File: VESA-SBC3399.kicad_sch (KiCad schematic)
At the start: 0 parts

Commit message: generate schematic
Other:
- added sheet CPU-RK3399 (CPU-RK3399.kicad_sch)
- added sheet Camera (Camera.kicad_sch)
- added sheet Ethernet PHY (PHY.kicad_sch)
- added sheet HDMI Port (HDMI.kicad_sch)
- added sheet PCIe M.2 M-Key (PCIe.kicad_sch)
- added sheet USB 2.0 Type-A0 (USBA0.kicad_sch)
- added sheet USB 2.0 Type-A1 (USBA1.kicad_sch)
- added sheet USB 3.0 Type-C0 (USBC0.kicad_sch)
- added sheet USB 3.0 Type-C1 (USBC1.kicad_sch)
- added sheet micro SD Card (microSD.kicad_sch)
- title: (none) -> VESA-SBC3399

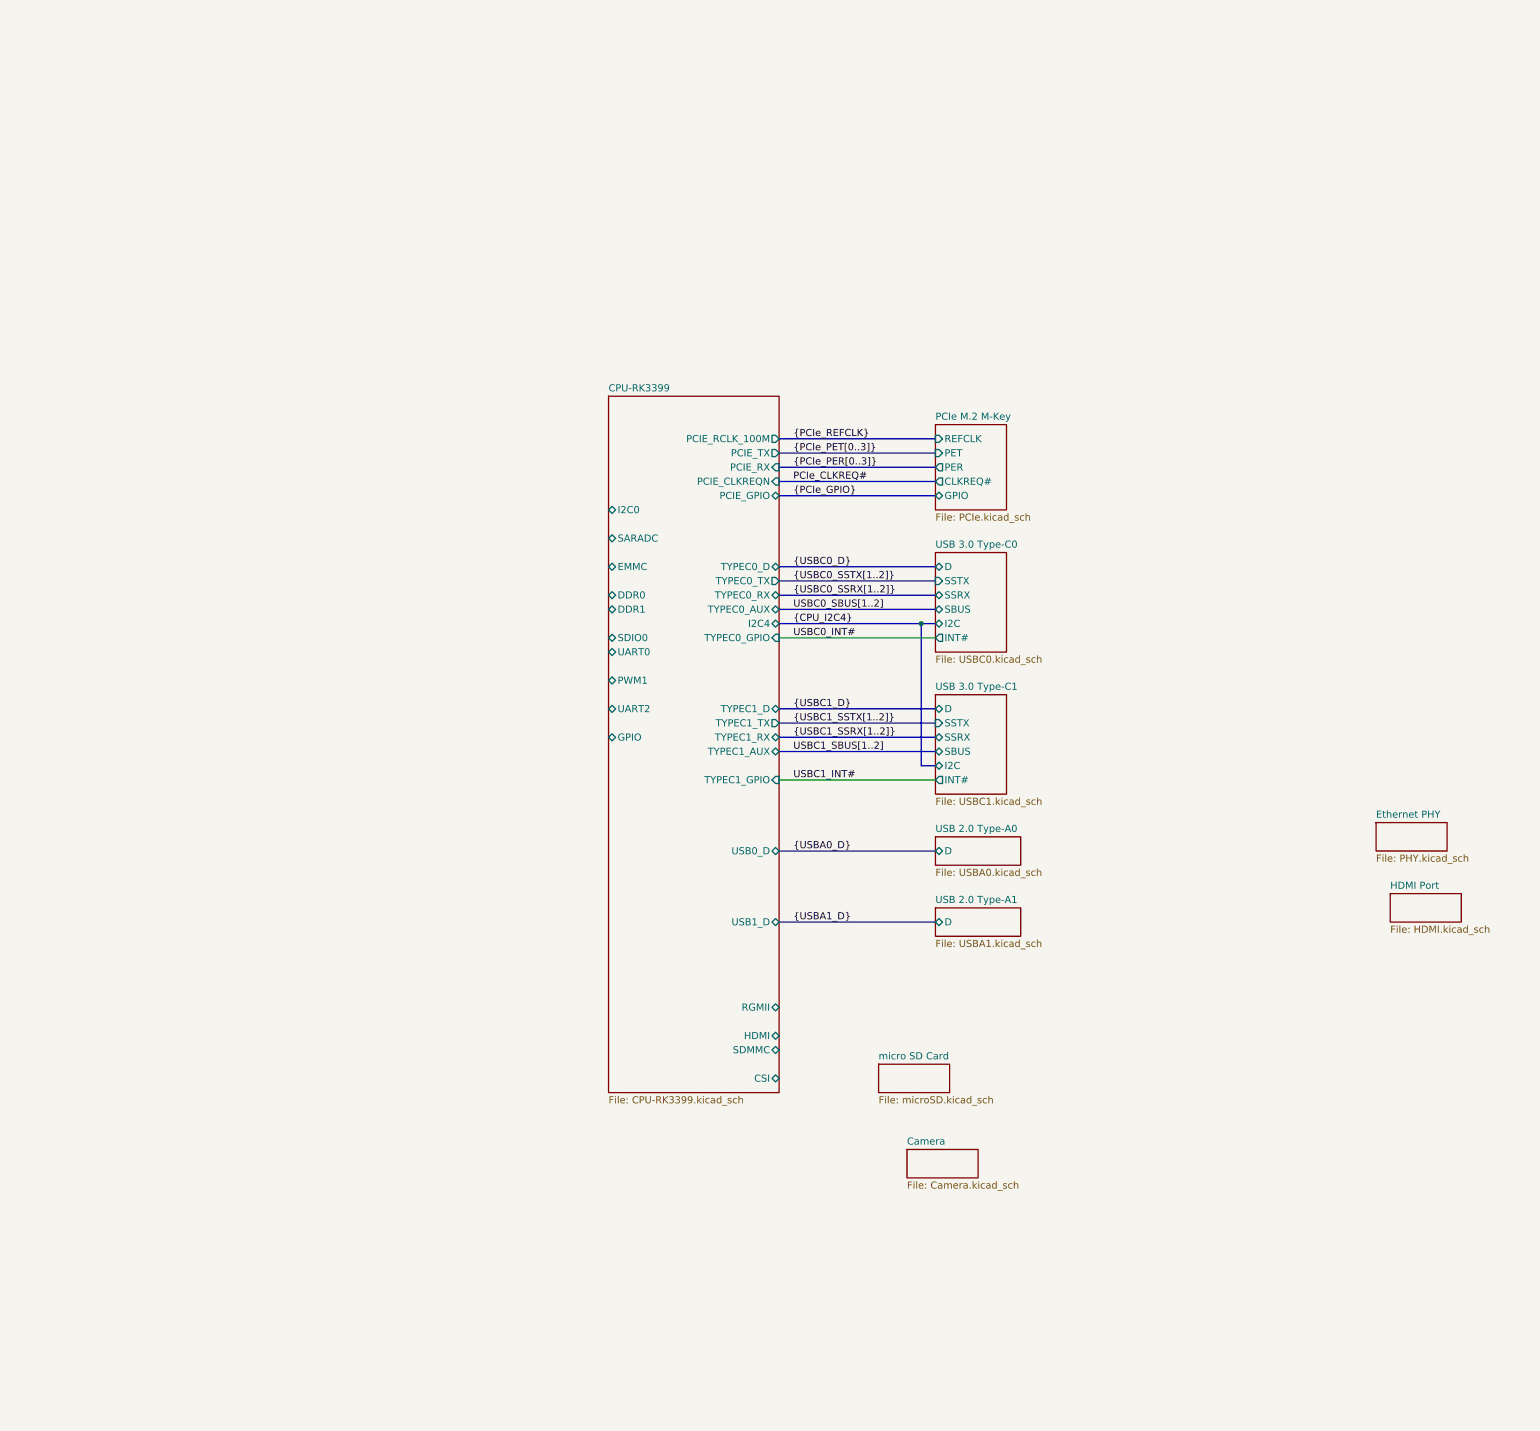
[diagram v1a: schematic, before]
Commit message: update schematic
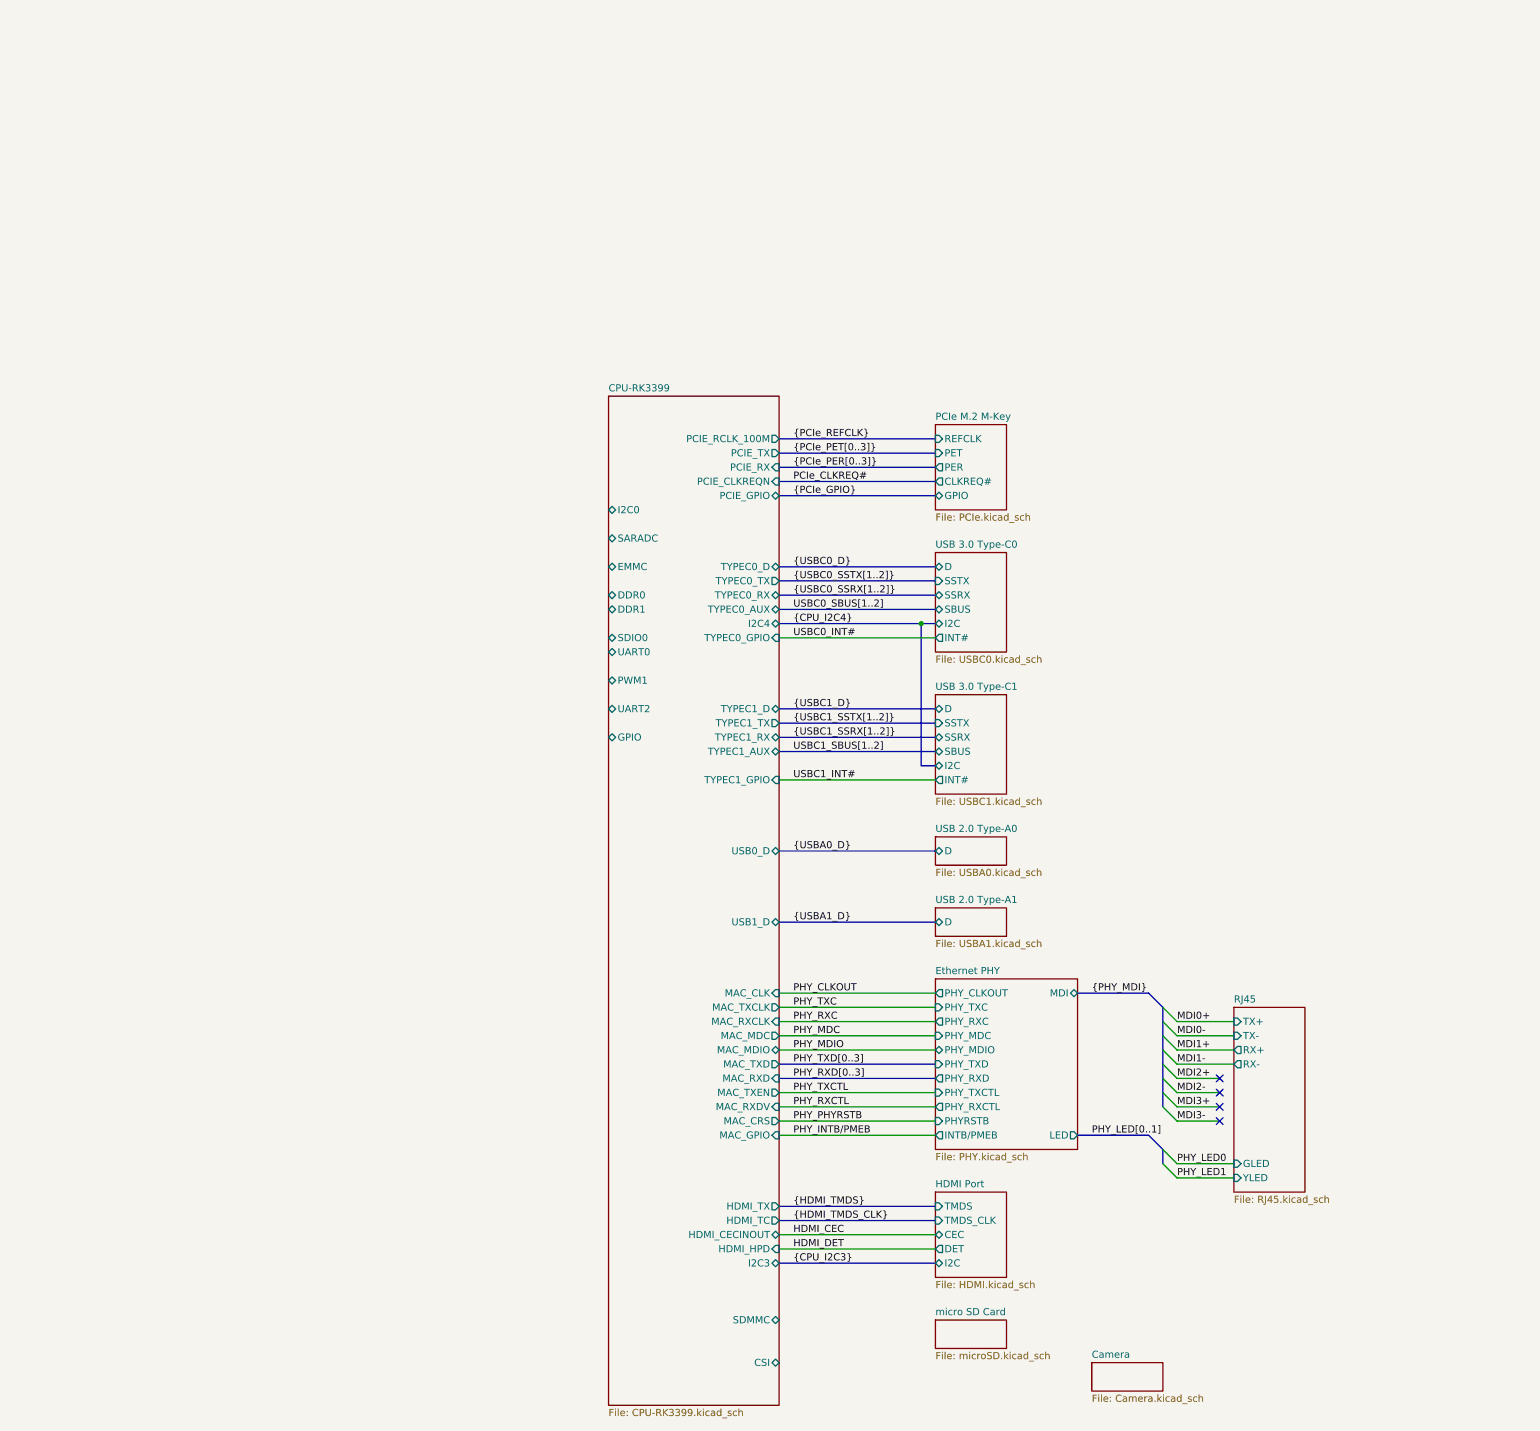
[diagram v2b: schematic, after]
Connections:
- no-connect marks 0 -> 4
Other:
- added sheet RJ45 (RJ45.kicad_sch)
- sheet CPU-RK3399 ports: added HDMI_CECINOUT, HDMI_HPD, HDMI_TC, HDMI_TX, I2C3, MAC_CLK, MAC_CRS, MAC_GPIO, MAC_MDC, MAC_MDIO, MAC_RXCLK, MAC_RXD, MAC_RXDV, MAC_TXCLK, MAC_TXD, MAC_TXEN; removed HDMI, RGMII
- sheet Ethernet PHY ports: added INTB/PMEB, LED, MDI, PHYRSTB, PHY_CLKOUT, PHY_MDC, PHY_MDIO, PHY_RXC, PHY_RXCTL, PHY_RXD, PHY_TXC, PHY_TXCTL, PHY_TXD; removed none
- sheet HDMI Port ports: added CEC, DET, I2C, TMDS, TMDS_CLK; removed none

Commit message: update root schematic
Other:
- added sheet Cooling Fan (FAN.kicad_sch)
- added sheet DDR3L RAM0 (RAM0.kicad_sch)
- added sheet DDR3L RAM1 (RAM1.kicad_sch)
- added sheet Power (Power.kicad_sch)
- added sheet WiFi_BLE (WiFi_BLE.kicad_sch)
- added sheet eMMC Flash (eMMC.kicad_sch)
- sheet CPU-RK3399 ports: added CAM_GPIO, DDR0_A, DDR0_BA, DDR0_CASN, DDR0_CKE, DDR0_CLK, DDR0_CSN, DDR0_DM, DDR0_DQ, DDR0_DQS, DDR0_ODT, DDR0_RASN, DDR0_RESETN, DDR0_WEN, DDR1_A, DDR1_BA, DDR1_CASN, DDR1_CKE, DDR1_CLK, DDR1_CSN, DDR1_DM, DDR1_DQ, DDR1_DQS, DDR1_ODT, DDR1_RASN, DDR1_RESETN, DDR1_WEN, EMMC_CLK, EMMC_CMD, EMMC_DATA, EMMC_STRB, FAN_GPIO, I2C1, MIPI_RX0_CLK, MIPI_RX0_D, SDMMC0_CLKOUT, SDMMC0_CMD, SDMMC0_D, SDMMC0_DET#, WLBT_GPIO; removed CSI, DDR0, DDR1, SDMMC
- sheet Camera ports: added CSI1_D, DSI_C, I2C, MCLK, PDN, RST; removed none
- sheet micro SD Card ports: added CD, CLX, CMD, DAT; removed none

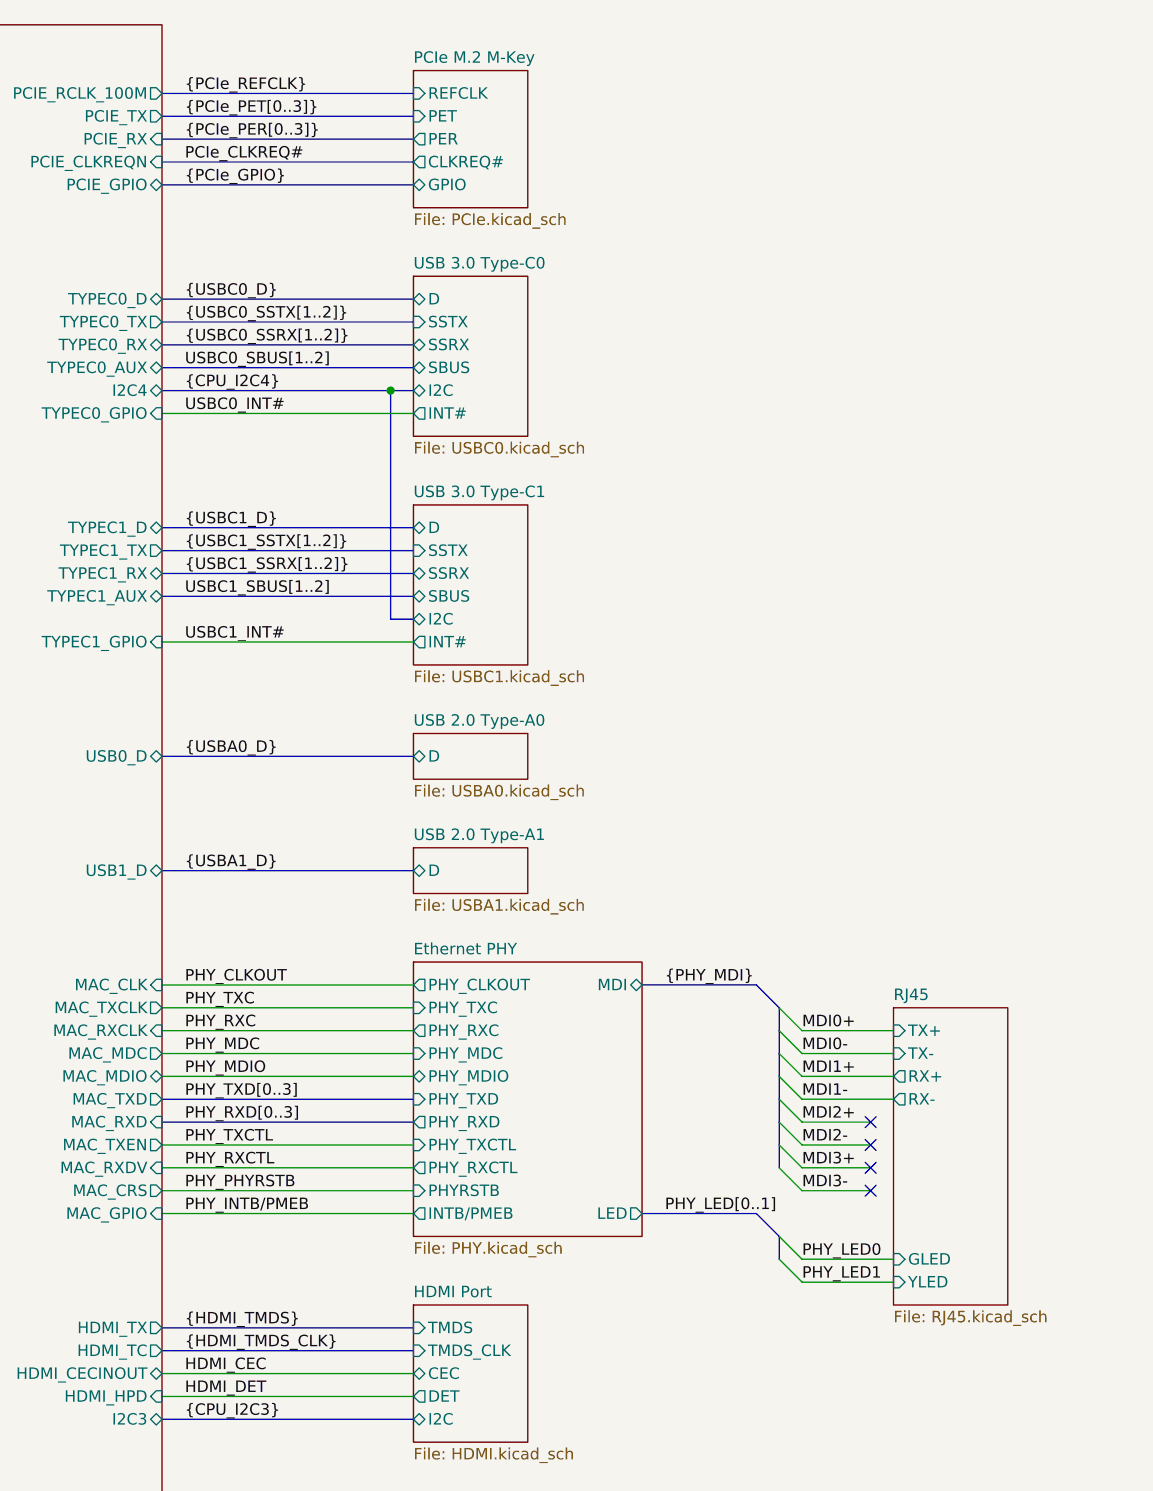
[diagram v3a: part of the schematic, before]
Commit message: create netclass
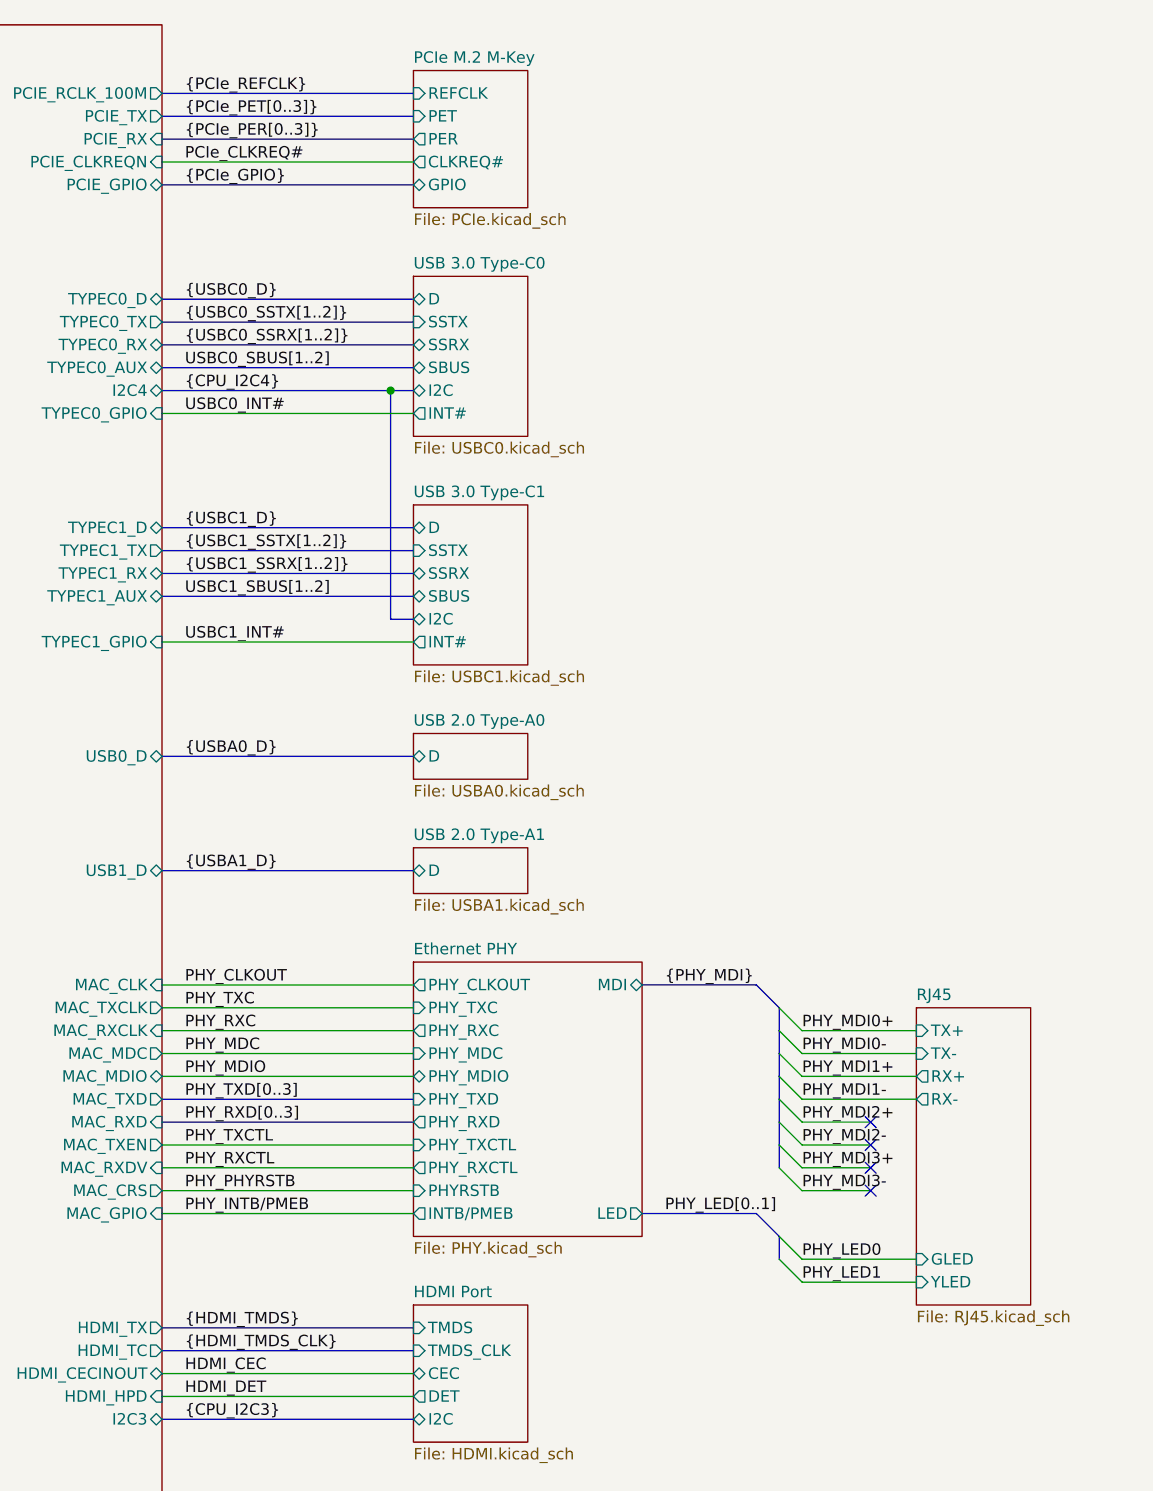
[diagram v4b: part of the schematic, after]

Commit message: design CPU Power
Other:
- sheet CPU-RK3399 ports: added VDD_CPU_B_FB, VDD_GPU_FB; removed none
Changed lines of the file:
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@@
 	(wire
 		(pts
+			(xy 172.72 33.02) (xy 175.26 33.02)
+		)
+		(stroke
+			(width 0)
+			(type default)
+		)
+	)
+	(wire
+		(pts
 			(xy 279.4 139.7) (xy 292.1 139.7)
 		)
@@
 		)
 	)
+	(wire
+		(pts
+			(xy 172.72 30.48) (xy 175.26 30.48)
+		)
+		(stroke
+			(width 0)
+			(type default)
+		)
+	)
 	(bus
 		(pts
@@
 		)
 	)
+	(label "VDD_GPU_FB"
+		(at 172.72 33.02 180)
+		(effects
+			(font
+				(size 1.27 1.27)
+			)
+			(justify right bottom)
+		)
+	)
 	(label "RAM0_CS#[0..3]"
 		(at 172.72 165.1 180)
@@
 		)
 	)
+	(label "VDD_CPU_B_FB"
+		(at 172.72 30.48 180)
+		(effects
+			(font
+				(size 1.27 1.27)
+			)
+			(justify right bottom)
+		)
+	)
 	(label "MSD_CMD"
 		(at 210.82 198.12 0)
@@
 			(effects
 				(font
+					(size 1.27 1.27)
+				)
+				(justify left)
+			)
+		)
+		(pin "VDD_CPU_B_FB" output
+			(at 175.26 30.48 180)
+			(effects
+				(font
+					(size 1.27 1.27)
+				)
+				(justify left)
+			)
+		)
+		(pin "VDD_GPU_FB" output
+			(at 175.26 33.02 180)
+			(effects
+				(font
